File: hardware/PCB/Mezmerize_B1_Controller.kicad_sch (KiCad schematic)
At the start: 47 parts, among them J1 230 Vac, J10 I2C DISPLAY (OLED/LCD), J11 I2C (FUTURE USE), J12 ROTARY ENC & SWITCH 1, J13 ROTARY ENC & SWITCH 2, J14 IR RECV, J2 B1 Relays, J3 PWR AMP L 12V TRIGGER, J4 PWR AMP L SWITCH, J5 PWR AMP R 12V TRIGGER, J6 PWR AMP R SWITCH, J7 PWR AMP TEMP NTC L, J8 PWR AMP TEMP NTC R, J9 MUSES 72320 (SPI), U1 AGQ20T03, U2 AGQ20T03, U3 ULN2803ADWR, U4 L7808CV, U5 MCP23008-E_SO, U6 24C02C_SN

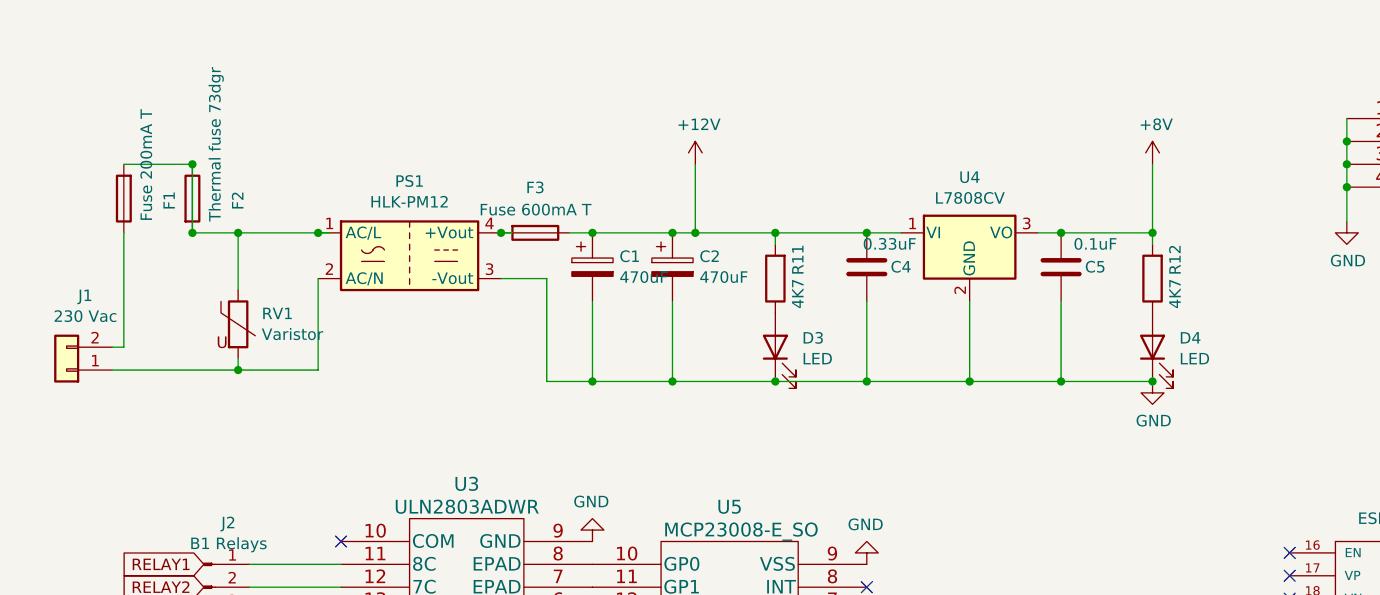
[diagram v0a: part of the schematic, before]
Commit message: PCB split
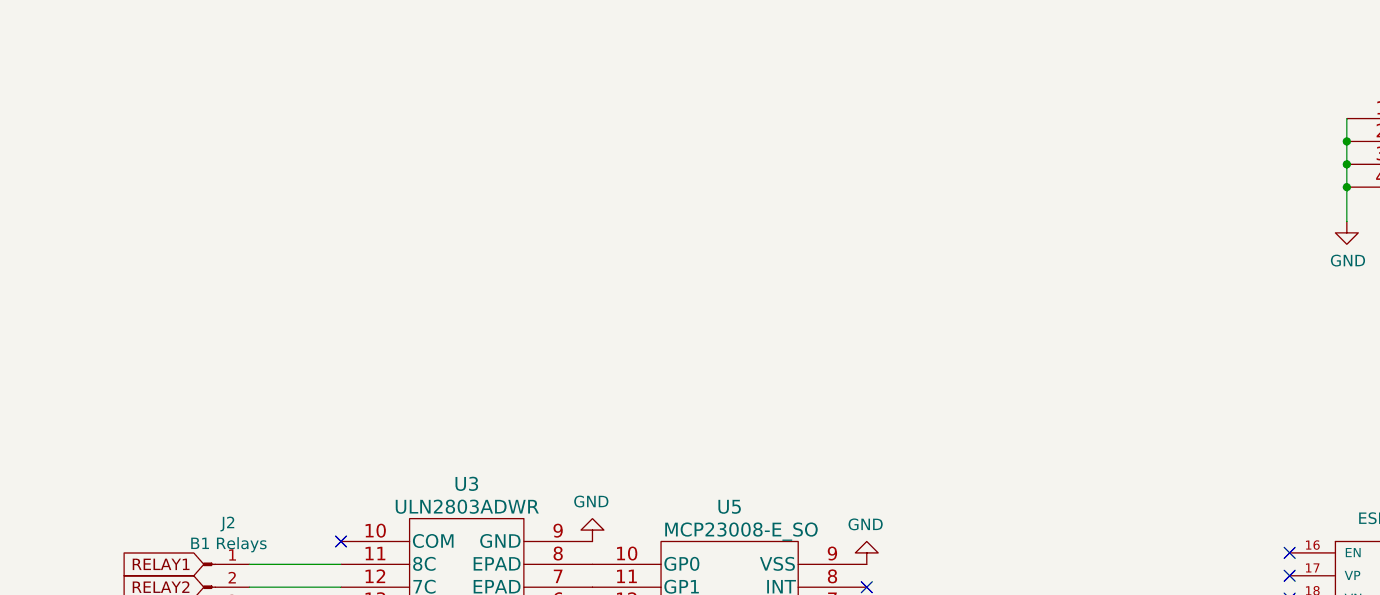
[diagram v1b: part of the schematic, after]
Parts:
- removed C1, C2: 470uF, Capacitor_THT:CP_Radial_D10.0mm_P5.00mm, symbol Mezmerize_B1_Controller-rescue:CP-Device
- removed C4: 0.33uF, Capacitor_SMD:C_0805_2012Metric_Pad1.15x1.40mm_HandSolder, symbol Device:C
- removed C5: 0.1uF, Capacitor_SMD:C_0805_2012Metric_Pad1.15x1.40mm_HandSolder, symbol Device:C
- removed D3, D4: LED, LED_SMD:LED_0805_2012Metric_Pad1.15x1.40mm_HandSolder, symbol Device:LED
- removed F1: Fuse 200mA T, B1 Mezmerize Controller:BLX-A, symbol Device:Fuse
- removed F2: Thermal fuse 73dgr, Resistor_THT:R_Axial_DIN0414_L11.9mm_D4.5mm_P15.24mm_Horizontal, symbol Device:Fuse
- removed F3: Fuse 600mA T, B1 Mezmerize Controller:BLX-A, symbol Device:Fuse
- removed J1: 230 Vac, TerminalBlock:TerminalBlock_bornier-2_P5.08mm, symbol Connector_Generic:Conn_01x02
- removed PS1: HLK-PM12, Converter_ACDC:Converter_ACDC_HiLink_HLK-PMxx, symbol Converter_ACDC:HLK-PM01
- removed R11, R12: 4K7, Resistor_SMD:R_0805_2012Metric_Pad1.15x1.40mm_HandSolder, symbol Device:R
- removed RV1: Varistor, Varistor:RV_Disc_D21.5mm_W4.6mm_P10mm, symbol Device:Varistor
- removed U4: L7808CV, Package_TO_SOT_THT:TO-220-3_Vertical, symbol Regulator_Linear:LM7808_TO220

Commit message: Missing changes ??
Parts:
- removed R1, R3: 10K, Resistor_SMD:R_0805_2012Metric_Pad1.15x1.40mm_HandSolder, symbol Device:R
- removed R2, R4: 5K, Resistor_SMD:R_0805_2012Metric_Pad1.15x1.40mm_HandSolder, symbol Device:R
- added J14: 12V, TerminalBlock:TerminalBlock_bornier-2_P5.08mm, symbol Connector_Generic:Conn_01x02
- added J15: 8V, TerminalBlock:TerminalBlock_bornier-2_P5.08mm, symbol Connector_Generic:Conn_01x02
- gave numbers to parts that had none: 1
- renumbered C3 to C1, J2 to J1, J11 to J10, J12 to J11, J13 to J12, J14 to J13, J3 to J2, J4 to J3, J5 to J4, J6 to J5, J7 to J6, J8 to J7, J9 to J8, J10 to J9, R9 to R1, R5 to R10, R10 to R4, R6 to R9, U5 to U4, U6 to U5
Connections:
- net +12V: now also J14.2 (Pin_2)
- net +8V: now also J15.2 (Pin_2)
- net GND: now also U6.2 (GND), J14.1 (Pin_1), J15.1 (Pin_1)
- net L_MEASURE_ON_OFF: no longer names the net of U6.5 (D4)
- net R_MEASURE_ON_OFF: no longer names the net of U6.3 (D15)
- no-connect marks 11 -> 17

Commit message: mod psu + control v 0.25
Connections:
- net +12V: now also J14.1 (Pin_1); no longer J14.2 (Pin_2)
- net +8V: now also J15.1 (Pin_1); no longer J15.2 (Pin_2)
- net GND: now also J14.2 (Pin_2), J15.2 (Pin_2); no longer J14.1 (Pin_1), J15.1 (Pin_1)
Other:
- moved on the sheet: J15
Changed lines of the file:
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@@
+    (stroke (width 0) (type default) (color 0 0 0 0))
+  )
+  (wire (pts (xy 78.74 34.29) (xy 78.74 35.56))
     (stroke (width 0) (type default) (color 0 0 0 0))
   )
@@
     (stroke (width 0) (type default) (color 0 0 0 0))
   )
+  (wire (pts (xy 78.74 35.56) (xy 80.01 35.56))
+    (stroke (width 0) (type default) (color 0 0 0 0))
+  )
   (wire (pts (xy 35.56 90.17) (xy 41.91 90.17))
     (stroke (width 0) (type default) (color 0 0 0 0))
@@
     (stroke (width 0) (type default) (color 0 0 0 0))
   )
-  (wire (pts (xy 120.65 35.56) (xy 127 35.56))
-    (stroke (width 0) (type default) (color 0 0 0 0))
-  )
   (wire (pts (xy 60.96 163.83) (xy 66.04 163.83))
     (stroke (width 0) (type default) (color 0 0 0 0))
   )
+  (wire (pts (xy 102.87 35.56) (xy 104.14 35.56))
+    (stroke (width 0) (type default) (color 0 0 0 0))
+  )
   (wire (pts (xy 60.96 138.43) (xy 60.96 163.83))
     (stroke (width 0) (type default) (color 0 0 0 0))
@@
     (stroke (width 0) (type default) (color 0 0 0 0))
   )
-  (wire (pts (xy 76.2 34.29) (xy 72.39 34.29))
-    (stroke (width 0) (type default) (color 0 0 0 0))
-  )
   (wire (pts (xy 31.75 134.62) (xy 27.94 134.62))
     (stroke (width 0) (type default) (color 0 0 0 0))
@@
     (stroke (width 0) (type default) (color 0 0 0 0))
   )
+  (wire (pts (xy 76.2 35.56) (xy 76.2 34.29))
+    (stroke (width 0) (type default) (color 0 0 0 0))
+  )
   (wire (pts (xy 87.63 104.14) (xy 86.36 104.14))
     (stroke (width 0) (type default) (color 0 0 0 0))
@@
     (stroke (width 0) (type default) (color 0 0 0 0))
   )
+  (wire (pts (xy 74.93 35.56) (xy 76.2 35.56))
+    (stroke (width 0) (type default) (color 0 0 0 0))
+  )
+  (wire (pts (xy 100.33 35.56) (xy 100.33 34.29))
+    (stroke (width 0) (type default) (color 0 0 0 0))
+  )
   (wire (pts (xy 41.91 87.63) (xy 52.07 87.63))
     (stroke (width 0) (type default) (color 0 0 0 0))
@@
     (stroke (width 0) (type default) (color 0 0 0 0))
   )
-  (wire (pts (xy 129.54 35.56) (xy 129.54 46.99))
-    (stroke (width 0) (type default) (color 0 0 0 0))
-  )
   (wire (pts (xy 106.68 111.76) (xy 106.68 119.38))
     (stroke (width 0) (type default) (color 0 0 0 0))
@@
     (stroke (width 0) (type default) (color 0 0 0 0))
   )
+  (wire (pts (xy 102.87 34.29) (xy 102.87 35.56))
+    (stroke (width 0) (type default) (color 0 0 0 0))
+  )
   (wire (pts (xy 80.01 95.25) (xy 80.01 100.33))
     (stroke (width 0) (type default) (color 0 0 0 0))
@@
     (stroke (width 0) (type default) (color 0 0 0 0))
   )
+  (wire (pts (xy 99.06 35.56) (xy 100.33 35.56))
+    (stroke (width 0) (type default) (color 0 0 0 0))
+  )
   (wire (pts (xy 163.83 25.4) (xy 163.83 27.94))
     (stroke (width 0) (type default) (color 0 0 0 0))
@@
   )
   (wire (pts (xy 80.01 100.33) (xy 87.63 100.33))
-    (stroke (width 0) (type default) (color 0 0 0 0))
-  )
-  (wire (pts (xy 78.74 34.29) (xy 78.74 46.99))
     (stroke (width 0) (type default) (color 0 0 0 0))
   )
@@
   (symbol (lib_id "Connector_Generic:Conn_01x02") (at 76.2 29.21 90) (unit 1)
     (in_bom yes) (on_board yes)
-    (property "Reference" "J14" (id 0) (at 84.455 31.2928 0))
-    (property "Value" "12V" (id 1) (at 82.1436 31.2928 0))
+    (property "Reference" "J14" (id 0) (at 77.47 24.3586 90))
+    (property "Value" "12V" (id 1) (at 77.47 26.67 90))
     (property "Footprint" "TerminalBlock:TerminalBlock_bornier-2_P5.08mm" (id 2) (at 76.2 29.21 0)
       (effects (font (size 1.27 1.27)) hide)
@@
     (pin "9")
   )
-  (symbol (lib_id "power:+8V") (at 129.54 46.99 270) (unit 1)
-    (in_bom yes) (on_board yes)
-    (property "Reference" "#PWR0103" (id 0) (at 125.73 46.99 0)
-      (effects (font (size 1.27 1.27)) hide)
-    )
-    (property "Value" "+8V" (id 1) (at 133.9342 47.371 0))
-    (property "Footprint" "" (id 2) (at 129.54 46.99 0)
-      (effects (font (size 1.27 1.27)) hide)
-    )
-    (property "Datasheet" "" (id 3) (at 129.54 46.99 0)
+  (symbol (lib_id "power:+8V") (at 99.06 35.56 90) (unit 1)
+    (in_bom yes) (on_board yes)
+    (property "Reference" "#PWR0103" (id 0) (at 102.87 35.56 0)
+      (effects (font (size 1.27 1.27)) hide)
+    )
+    (property "Value" "+8V" (id 1) (at 93.98 35.56 90))
+    (property "Footprint" "" (id 2) (at 99.06 35.56 0)
+      (effects (font (size 1.27 1.27)) hide)
+    )
+    (property "Datasheet" "" (id 3) (at 99.06 35.56 0)
       (effects (font (size 1.27 1.27)) hide)
     )
@@
     (pin "1")
   )
-  (symbol (lib_id "Connector_Generic:Conn_01x02") (at 127 30.48 90) (unit 1)
-    (in_bom yes) (on_board yes)
-    (property "Reference" "J15" (id 0) (at 135.255 32.5628 0))
-    (property "Value" "8V" (id 1) (at 132.9436 32.5628 0))
-    (property "Footprint" "TerminalBlock:TerminalBlock_bornier-2_P5.08mm" (id 2) (at 127 30.48 0)
-      (effects (font (size 1.27 1.27)) hide)
-    )
-    (property "Datasheet" "~" (id 3) (at 127 30.48 0)
-      (effects (font (size 1.27 1.27)) hide)
-    )
-    (pin "1")
-    (pin "2")
-  )
-  (symbol (lib_id "power:GND") (at 120.65 35.56 270) (unit 1)
+  (symbol (lib_id "Connector_Generic:Conn_01x02") (at 100.33 29.21 90) (unit 1)
+    (in_bom yes) (on_board yes)
+    (property "Reference" "J15" (id 0) (at 101.6 24.3586 90))
+    (property "Value" "8V" (id 1) (at 101.6 26.67 90))
+    (property "Footprint" "TerminalBlock:TerminalBlock_bornier-2_P5.08mm" (id 2) (at 100.33 29.21 0)
+      (effects (font (size 1.27 1.27)) hide)
+    )
+    (property "Datasheet" "~" (id 3) (at 100.33 29.21 0)
+      (effects (font (size 1.27 1.27)) hide)
+    )
+    (pin "1")
+    (pin "2")
+  )
+  (symbol (lib_id "power:GND") (at 104.14 35.56 90) (unit 1)
     (in_bom yes) (on_board yes) (fields_autoplaced)
-    (property "Reference" "#PWR0102" (id 0) (at 114.3 35.56 0)
-      (effects (font (size 1.27 1.27)) hide)
-    )
-    (property "Value" "GND" (id 1) (at 117.4751 35.9938 90)
-      (effects (font (size 1.27 1.27)) (justify right))
-    )
-    (property "Footprint" "" (id 2) (at 120.65 35.56 0)
-      (effects (font (size 1.27 1.27)) hide)
-    )
-    (property "Datasheet" "" (id 3) (at 120.65 35.56 0)
+    (property "Reference" "#PWR0102" (id 0) (at 110.49 35.56 0)
+      (effects (font (size 1.27 1.27)) hide)
+    )
+    (property "Value" "GND" (id 1) (at 107.95 35.5599 90)
+      (effects (font (size 1.27 1.27)) (justify right))
+    )
+    (property "Footprint" "" (id 2) (at 104.14 35.56 0)
+      (effects (font (size 1.27 1.27)) hide)
+    )
+    (property "Datasheet" "" (id 3) (at 104.14 35.56 0)
       (effects (font (size 1.27 1.27)) hide)
     )
@@
     (pin "1")
   )
-  (symbol (lib_id "power:GND") (at 72.39 34.29 270) (unit 1)
+  (symbol (lib_id "power:GND") (at 80.01 35.56 90) (unit 1)
     (in_bom yes) (on_board yes) (fields_autoplaced)
-    (property "Reference" "#PWR0104" (id 0) (at 66.04 34.29 0)
-      (effects (font (size 1.27 1.27)) hide)
-    )
-    (property "Value" "GND" (id 1) (at 67.9466 34.29 0))
-    (property "Footprint" "" (id 2) (at 72.39 34.29 0)
-      (effects (font (size 1.27 1.27)) hide)
-    )
-    (property "Datasheet" "" (id 3) (at 72.39 34.29 0)
+    (property "Reference" "#PWR0104" (id 0) (at 86.36 35.56 0)
+      (effects (font (size 1.27 1.27)) hide)
+    )
+    (property "Value" "GND" (id 1) (at 83.82 35.5599 90)
+      (effects (font (size 1.27 1.27)) (justify right))
+    )
+    (property "Footprint" "" (id 2) (at 80.01 35.56 0)
+      (effects (font (size 1.27 1.27)) hide)
+    )
+    (property "Datasheet" "" (id 3) (at 80.01 35.56 0)
       (effects (font (size 1.27 1.27)) hide)
     )
@@
     (pin "1")
   )
-  (symbol (lib_id "power:+12V") (at 78.74 46.99 270) (unit 1)
-    (in_bom yes) (on_board yes)
-    (property "Reference" "#PWR0105" (id 0) (at 74.93 46.99 0)
-      (effects (font (size 1.27 1.27)) hide)
-    )
-    (property "Value" "+12V" (id 1) (at 83.1342 47.371 0))
-    (property "Footprint" "" (id 2) (at 78.74 46.99 0)
-      (effects (font (size 1.27 1.27)) hide)
-    )
-    (property "Datasheet" "" (id 3) (at 78.74 46.99 0)
-      (effects (font (size 1.27 1.27)) hide)
-    )
+  (symbol (lib_id "power:+12V") (at 74.93 35.56 90) (unit 1)
+    (in_bom yes) (on_board yes)
+    (property "Reference" "#PWR0105" (id 0) (at 78.74 35.56 0)
+      (effects (font (size 1.27 1.27)) hide)
+    )
+    (property "Value" "+12V" (id 1) (at 68.58 35.56 90))
+    (property "Footprint" "" (id 2) (at 74.93 35.56 0)
+      (effects (font (size 1.27 1.27)) hide)
+    )
+    (property "Datasheet" "" (id 3) (at 74.93 35.56 0)
+      (effects (font (size 1.27 1.27)) hide)
+    )
